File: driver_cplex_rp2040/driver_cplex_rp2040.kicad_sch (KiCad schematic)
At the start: 0 parts

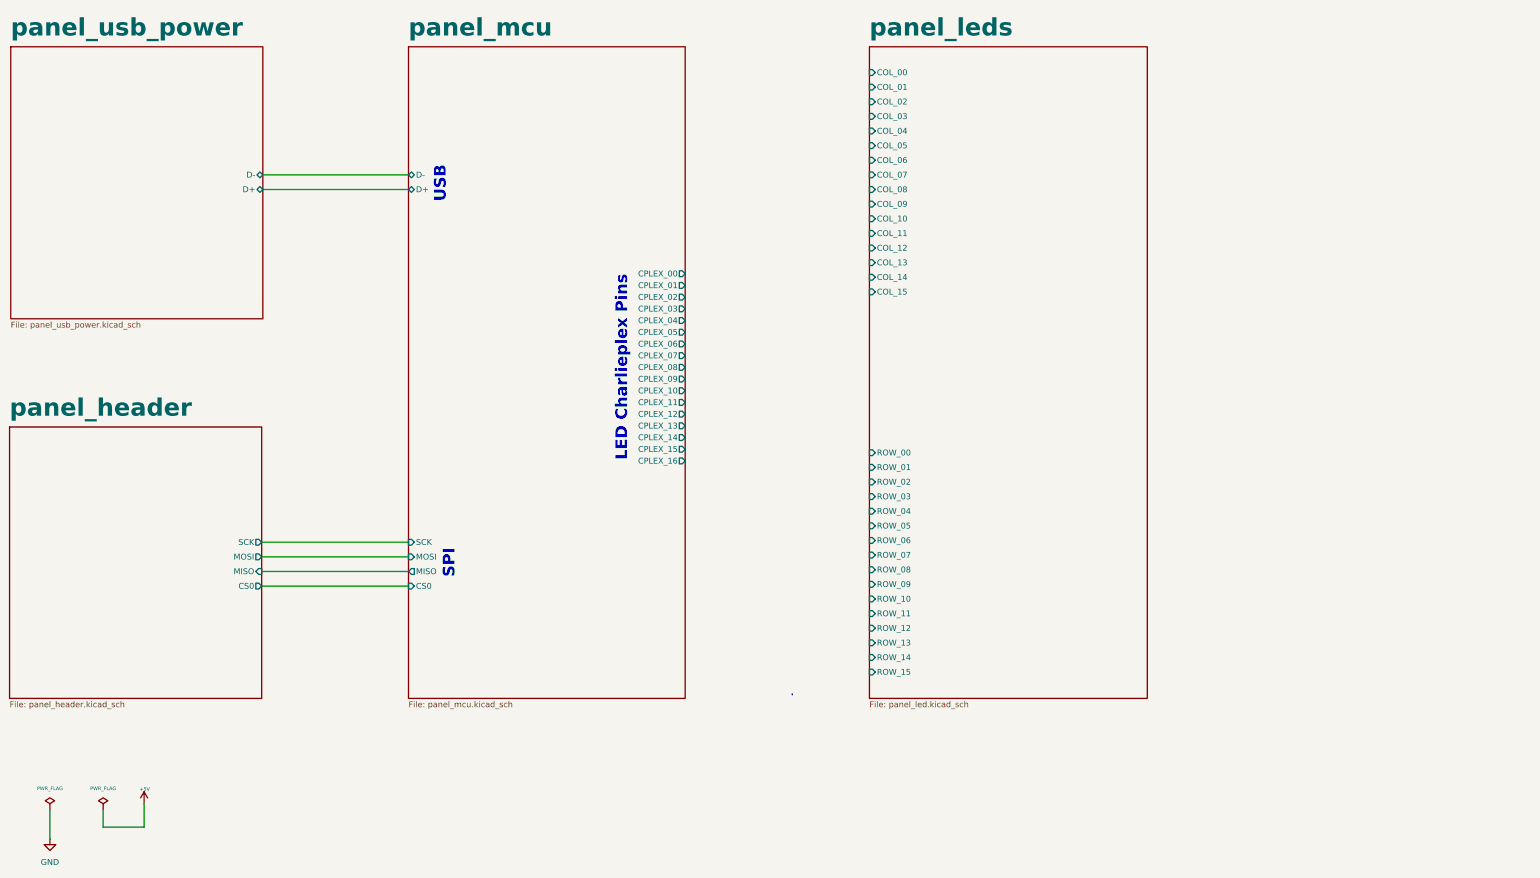
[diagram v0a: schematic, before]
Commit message: Added Charlieplexed version of rp2040 single pcb design.
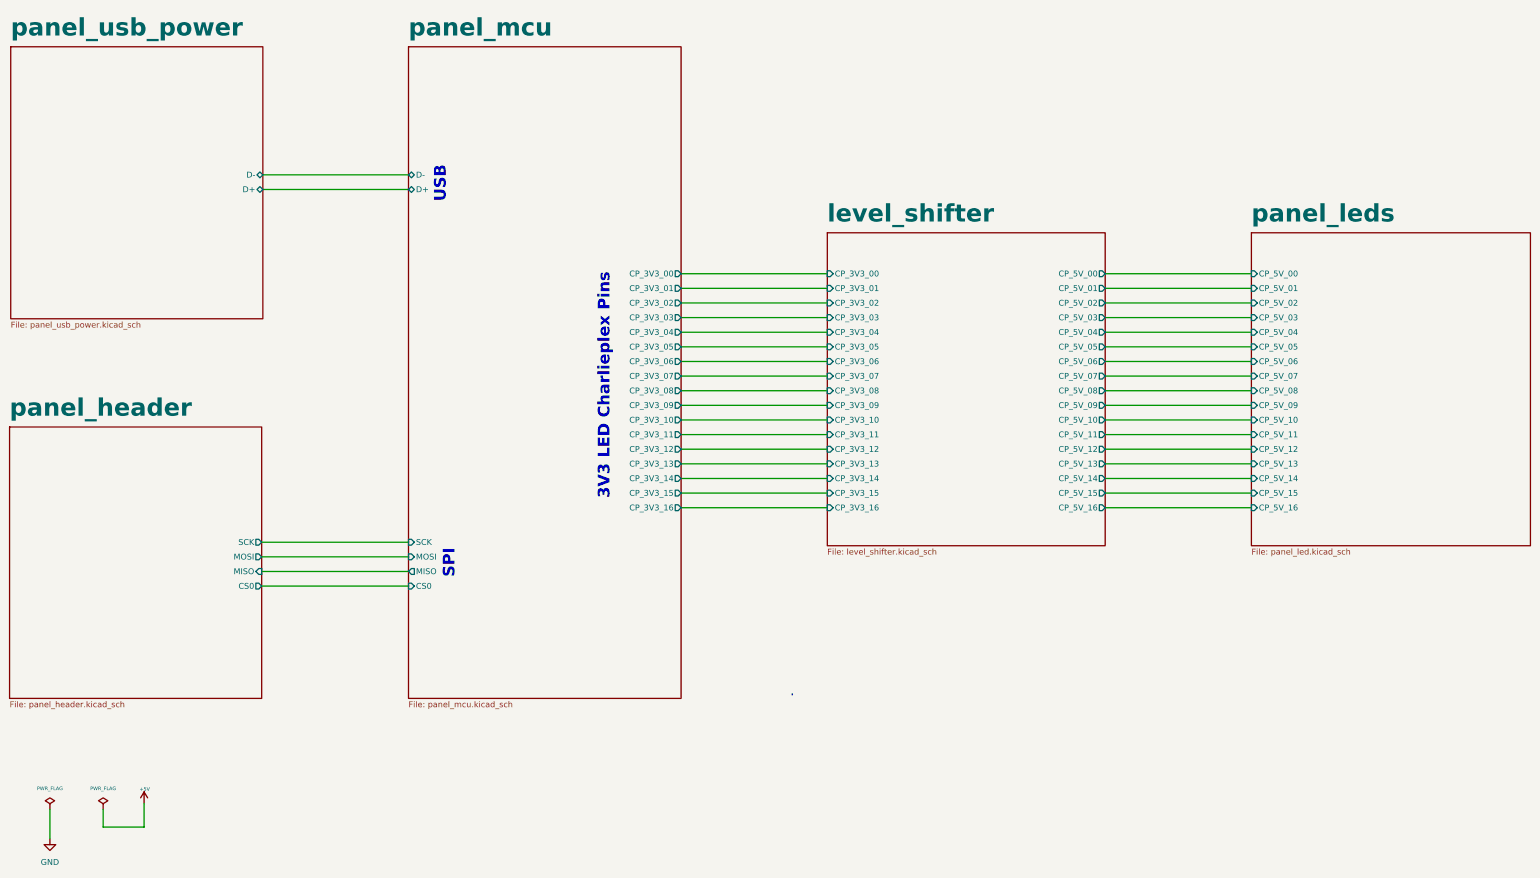
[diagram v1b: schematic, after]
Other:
- added sheet level_shifter (level_shifter.kicad_sch)
- sheet panel_leds ports: added CP_5V_00, CP_5V_01, CP_5V_02, CP_5V_03, CP_5V_04, CP_5V_05, CP_5V_06, CP_5V_07, CP_5V_08, CP_5V_09, CP_5V_10, CP_5V_11, CP_5V_12, CP_5V_13, CP_5V_14, CP_5V_15, CP_5V_16; removed COL_00, COL_01, COL_02, COL_03, COL_04, COL_05, COL_06, COL_07, COL_08, COL_09, COL_10, COL_11, COL_12, COL_13, COL_14, COL_15, ROW_00, ROW_01, ROW_02, ROW_03, ROW_04, ROW_05, ROW_06, ROW_07, ROW_08, ROW_09, ROW_10, ROW_11, ROW_12, ROW_13, ROW_14, ROW_15
- sheet panel_mcu ports: added CP_3V3_00, CP_3V3_01, CP_3V3_02, CP_3V3_03, CP_3V3_04, CP_3V3_05, CP_3V3_06, CP_3V3_07, CP_3V3_08, CP_3V3_09, CP_3V3_10, CP_3V3_11, CP_3V3_12, CP_3V3_13, CP_3V3_14, CP_3V3_15, CP_3V3_16; removed CPLEX_00, CPLEX_01, CPLEX_02, CPLEX_03, CPLEX_04, CPLEX_05, CPLEX_06, CPLEX_07, CPLEX_08, CPLEX_09, CPLEX_10, CPLEX_11, CPLEX_12, CPLEX_13, CPLEX_14, CPLEX_15, CPLEX_16
- note added: "3V3 LED Charlieplex Pins"
- note removed: "LED Charlieplex Pins"

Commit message: Worked on production files.
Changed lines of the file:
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@@
+    (stroke (width 0) (type default))
+  )
+  (wire (pts (xy 36.322 210.058) (xy 36.322 213.233))
     (stroke (width 0) (type default))
   )
@@
   )
   (wire (pts (xy 171.45 100.33) (xy 203.2 100.33))
-    (stroke (width 0) (type default))
-  )
-  (wire (pts (xy 34.417 210.312) (xy 34.417 216.662))
     (stroke (width 0) (type default))
   )
@@
     (effects (font (size 2.54 2.54) (thickness 0.254) bold) (justify left bottom))
   )
-  (symbol (lib_id "power:PWR_FLAG") (at 34.417 210.312 0) (unit 1)
+  (symbol (lib_id "power:GND") (at 36.322 213.233 0) (unit 1)
+    (in_bom yes) (on_board yes) (dnp no) (fields_autoplaced)
+    (property "Reference" "#PWR051" (at 36.322 219.583 0)
+      (effects (font (size 1.27 1.27)) hide)
+    )
+    (property "Value" "GND" (at 36.322 218.313 0)
+      (effects (font (size 1.27 1.27)))
+    )
+    (property "Footprint" "" (at 36.322 213.233 0)
+      (effects (font (size 1.27 1.27)) hide)
+    )
+    (property "Datasheet" "" (at 36.322 213.233 0)
+      (effects (font (size 1.27 1.27)) hide)
+    )
+    (pin "1")
+    (instances
+      (project "driver_cplex_rp2040"
+        (path "/1e634561-32a0-4ffa-9d4f-e93f355464d5"
+          (reference "#PWR051") (unit 1)
+        )
+      )
+    )
+  )
+  (symbol (lib_id "power:PWR_FLAG") (at 36.322 210.058 0) (unit 1)
     (in_bom yes) (on_board yes) (dnp no)
-    (property "Reference" "#FLG01" (at 34.417 207.899 0)
+    (property "Reference" "#FLG01" (at 36.322 207.645 0)
       (effects (font (size 0.762 0.762)) hide)
     )
-    (property "Value" "PWR_FLAG" (at 34.417 205.74 0)
+    (property "Value" "PWR_FLAG" (at 36.322 205.486 0)
       (effects (font (size 0.762 0.762)))
     )
-    (property "Footprint" "" (at 34.417 210.312 0)
+    (property "Footprint" "" (at 36.322 210.058 0)
       (effects (font (size 1.524 1.524)))
     )
-    (property "Datasheet" "" (at 34.417 210.312 0)
+    (property "Datasheet" "" (at 36.322 210.058 0)
       (effects (font (size 1.524 1.524)))
     )
@@
         )
       )
-    )
-  )
-  (symbol (lib_id "power:GND") (at 34.417 216.662 0) (unit 1)
-    (in_bom yes) (on_board yes) (dnp no) (fields_autoplaced)
-    (property "Reference" "#PWR051" (at 34.417 223.012 0)
-      (effects (font (size 1.27 1.27)) hide)
-    )
-    (property "Value" "GND" (at 34.417 221.742 0)
-      (effects (font (size 1.27 1.27)))
-    )
-    (property "Footprint" "" (at 34.417 216.662 0)
-      (effects (font (size 1.27 1.27)) hide)
-    )
-    (property "Datasheet" "" (at 34.417 216.662 0)
-      (effects (font (size 1.27 1.27)) hide)
-    )
-    (pin "1")
-    (instances
-      (project "driver_cplex_rp2040"
-        (path "/1e634561-32a0-4ffa-9d4f-e93f355464d5"
-          (reference "#PWR051") (unit 1)
-        )
-      )
